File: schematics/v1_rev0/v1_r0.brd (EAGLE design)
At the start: 34.1 x 45.1 mm, 46 parts, among them Q1 LPM2302, Q2 LPM2302, Q3 16MHz, U1 ATMEGA*, U2 TMP36F

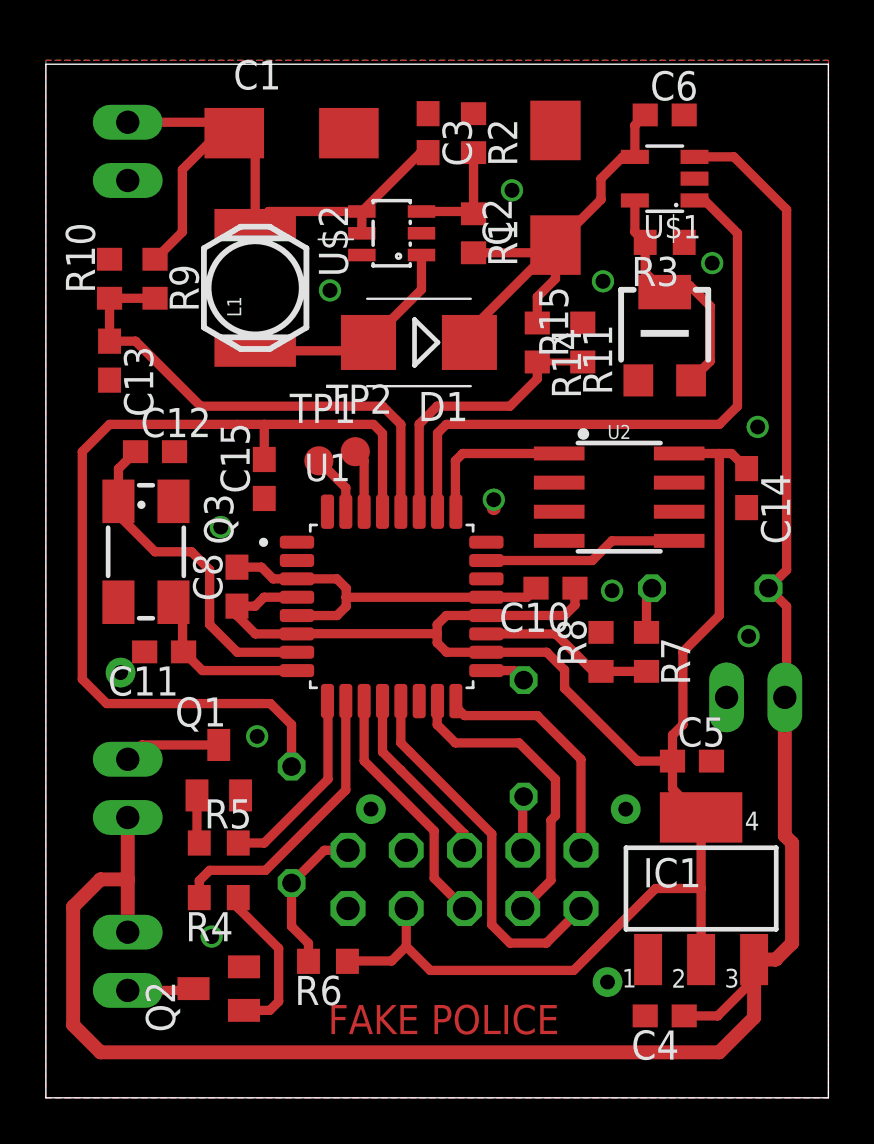
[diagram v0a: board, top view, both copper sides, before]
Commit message: even newser schematics
WARNING: replace AMS1117 with MAX8888
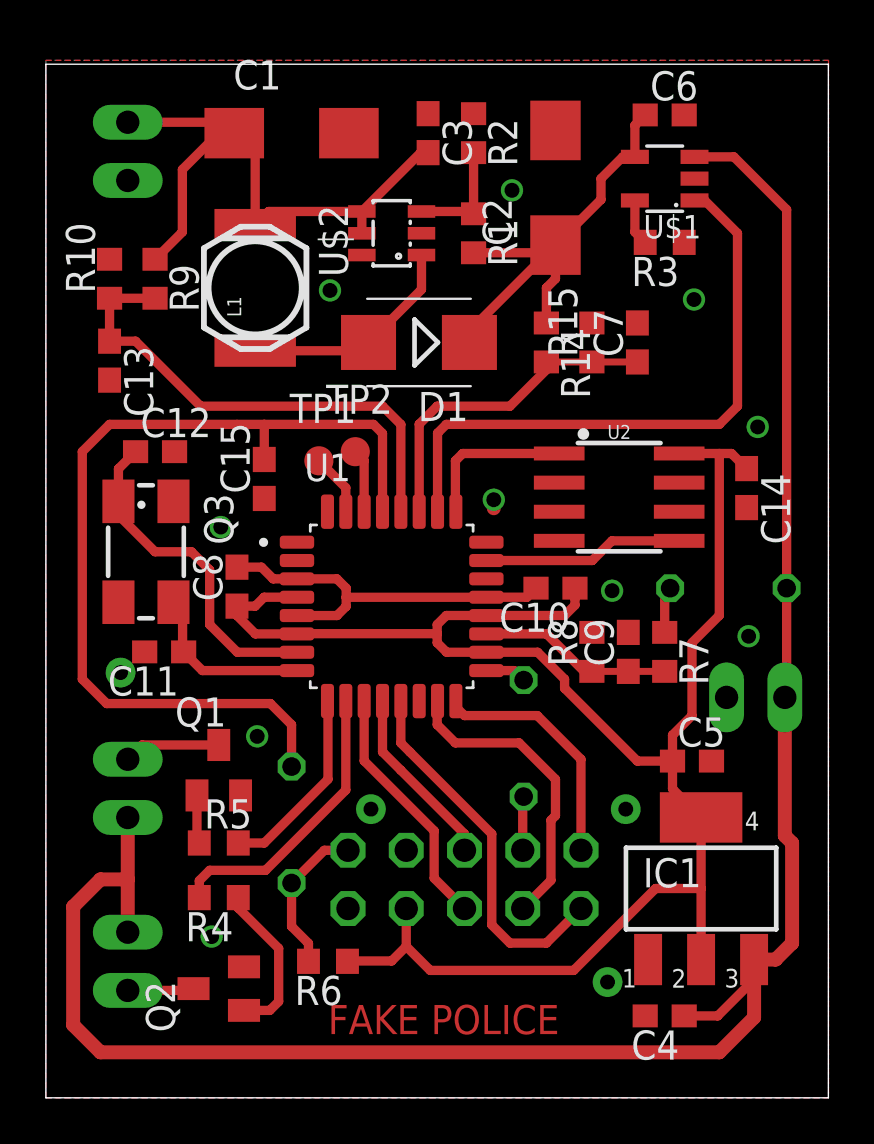
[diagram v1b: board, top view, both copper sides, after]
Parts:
- removed R11: 47k, resistor:RTRIMCVR42A
- added C7, C9: 100n, rcl:C0603
- Q3: value 16MHz -> 32.768 kHz
- R10, R14, R15, R9: value 47k -> 1M
- R3: value 10k -> 8k
- R7: value 47k -> 470k
- R8: value 100k -> 1M
- moved R16 0.79 mm to (29.8, 22.2)
- moved R7 0.79 mm to (27.0, 19.4)
- moved R14 0.40 mm to (21.8, 32.9)
- moved R15 0.40 mm to (23.8, 32.9)
- moved R8 0.40 mm to (23.8, 19.4)
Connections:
- net BOOSTVOL: now also C7.1
- net GND: now also C7.2, C9.2; no longer R11.1
- net N$1: no longer R11.2, R11.3
- net N$9: now also C9.1
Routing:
- net N$1: track 10.8 -> 2.01 mm
- net BOOSTVOL: track 12.5 -> 14.7 mm
- net N$9: track 7.68 -> 8.56 mm
- net +UB: track 89.8 -> 89.2 mm
- net GND: vias 15 -> 14
